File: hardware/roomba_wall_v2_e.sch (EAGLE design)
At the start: 11 parts, among them T1 BC846, U1 ATTINY45V-10SU

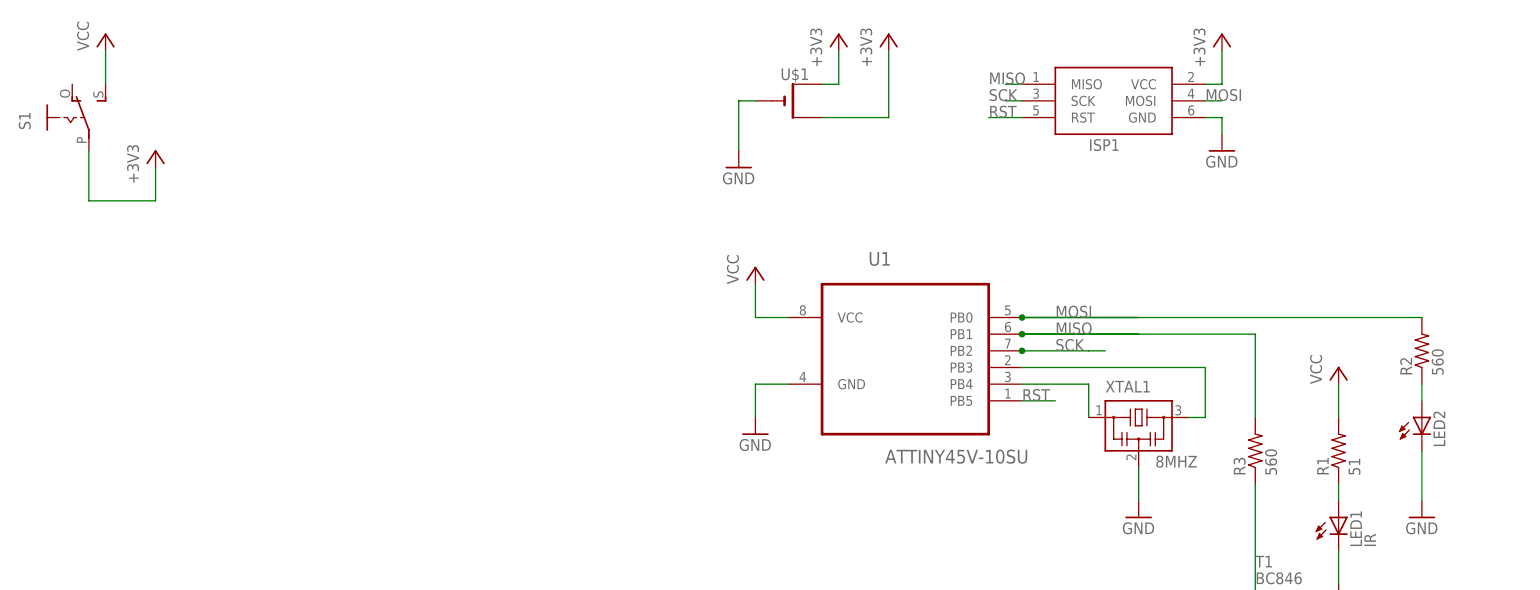
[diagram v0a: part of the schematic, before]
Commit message: Latest changes to rev E Not sure what's in here; they were made a while ago and just weren't committed.  This is possibly the fix to the unconnected GND on the MCU.
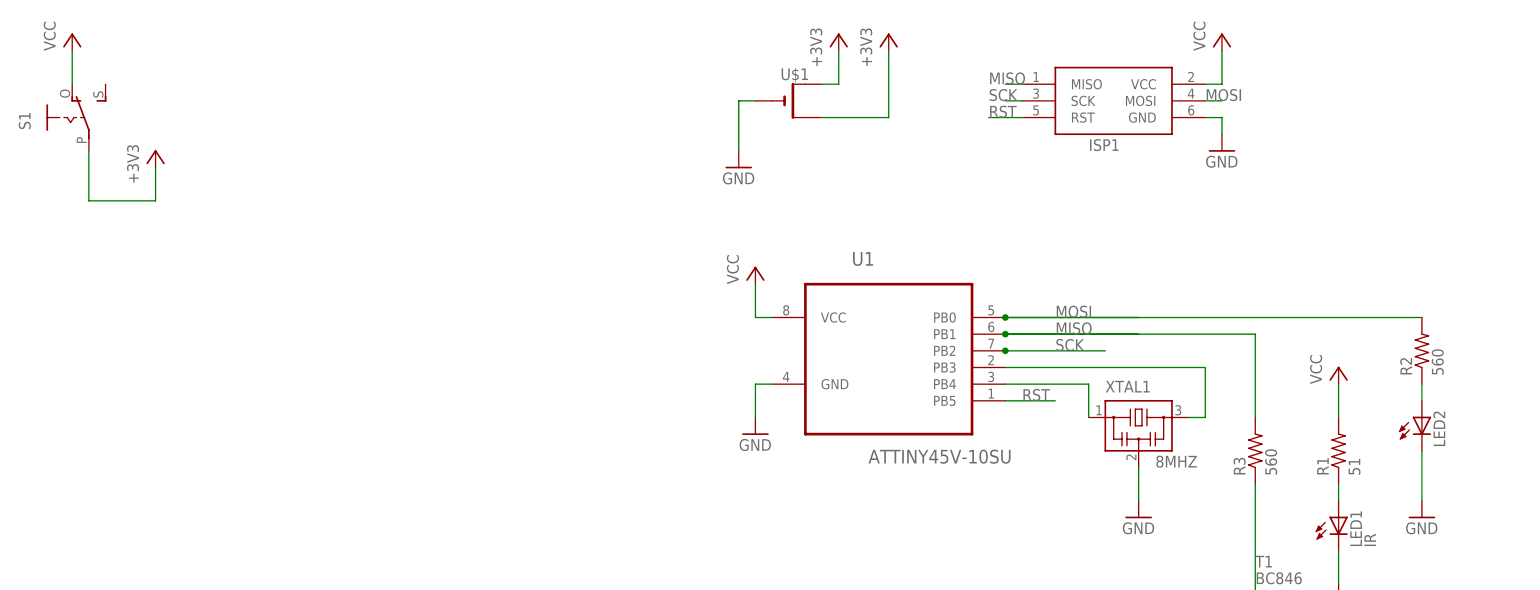
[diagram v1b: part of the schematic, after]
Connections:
- net +3V3: no longer ISP1.VCC
- net GND: now also U1.GND
- net VCC: now also ISP1.VCC, S1.O, U1.VCC; no longer S1.S
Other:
- moved on the sheet: U1
